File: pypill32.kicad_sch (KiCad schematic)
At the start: 32 parts, among them J1 HeaderR, J2 HeaderL, J3 ISP, U1 SRV05-4, U2 PY32F030F18P6, U3 CH340N

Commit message: intermediate save
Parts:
- removed JP1: PA8_ENA, Jumper:SolderJumper-2_P1.3mm_Open_RoundedPad1.0x1.5mm, symbol Jumper:SolderJumper_2_Open
- added D3: LED-R, LED_SMD:LED_0805_2012Metric_Pad1.15x1.40mm_HandSolder, symbol Device:LED
- added JP2: PA8_SEL, Jumper:SolderJumper-3_P1.3mm_Open_RoundedPad1.0x1.5mm, symbol Jumper:SolderJumper_3_Open
- added R7: 1k, Resistor_SMD:R_0805_2012Metric_Pad1.20x1.40mm_HandSolder, symbol Device:R_Small
- R1: value 1k -> 1.5k
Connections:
- net GND: now also D3.1 (K)
- net PA8: now also JP2.3 (B)
- net at U2.10 (PA8): now also JP2.2 (C)
- net USB_DM renamed USB_D-
- net USB_DP renamed USB_D+
- new net: D3.2 (A), R7.2
- new net: JP2.1 (A), R7.1
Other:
- note added: "TODO: ------ -3V3 regu/hakkuri -BOOT0/1 -nRT-kytkentä -RESET-nappi -ohjelmointiheaderi"

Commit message: intermediate save
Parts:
- removed H1: MountingHole_Pad_MP, MountingHole:MountingHole_2.7mm_M2.5_ISO7380_Pad, symbol Mechanical:MountingHole_Pad_MP
- removed J3: ISP, Connector_PinHeader_2.54mm:PinHeader_1x05_P2.54mm_Vertical, symbol Connector:Conn_01x05_Pin
- added H1: MountingHole, MountingHole:MountingHole_2.7mm_M2.5_ISO7380_Pad, symbol Mechanical:MountingHole
- added J4: ISP, Connector_PinHeader_2.54mm:PinHeader_1x04_P2.54mm_Vertical, symbol Connector:Conn_01x04_Pin
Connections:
- net +3V3: now also J4.4 (Pin_4)
- net GND: now also J4.1 (Pin_1)
- net PF0: now reaches J2.5 (Pin_5), R6.2, U2.1 (OSCIN-PF0)
- net PF1: now reaches J2.6 (Pin_6), R5.2, U2.2 (OSCOUT-PF1)
- net PF2-NRST: now reaches J2.7 (Pin_7), U2.3 (PF2-NRST)
- net PF3: now reaches J2.8 (Pin_8), U2.4 (PF3)
- net PA2: now reaches J2.9 (Pin_9), U2.5 (PA2)
- net PA3: now reaches J2.10 (Pin_10), U2.6 (PA3)
- net PA13 renamed SWDIO
- net SWDIO: now also J4.2 (Pin_2)
- net PA14 renamed SWDCLK
- net SWDCLK: now also J4.3 (Pin_3)
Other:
- note added: "TODO: ------ -SMD fuse -ferriitti? -3V3 regu/hakkuri -BOOT0/1 -nRT-kytkentä -RESET-nappi -alareunan maa ympäri -tarkasta ohjelmointiheaderi -optio 32k kiteelle? -bottomin labelit -ikonit -lisenssi"
- note removed: "TODO: ------ -3V3 regu/hakkuri -BOOT0/1 -nRT-kytkentä -RESET-nappi -ohjelmointiheaderi"

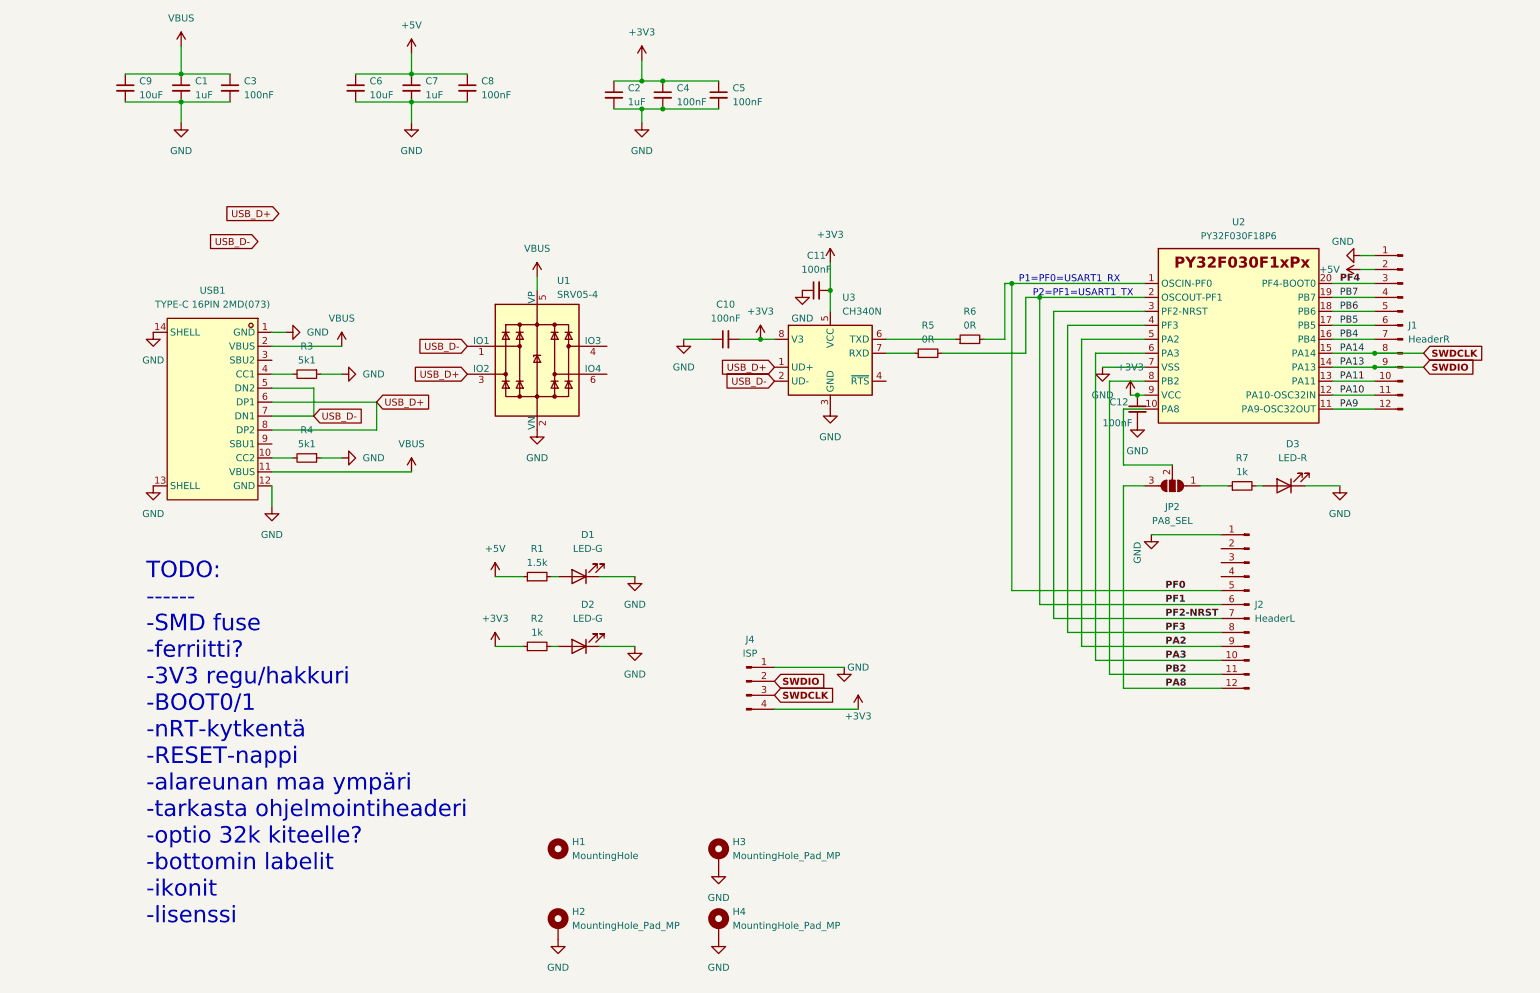
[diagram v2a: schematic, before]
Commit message: switch footprint and 3d
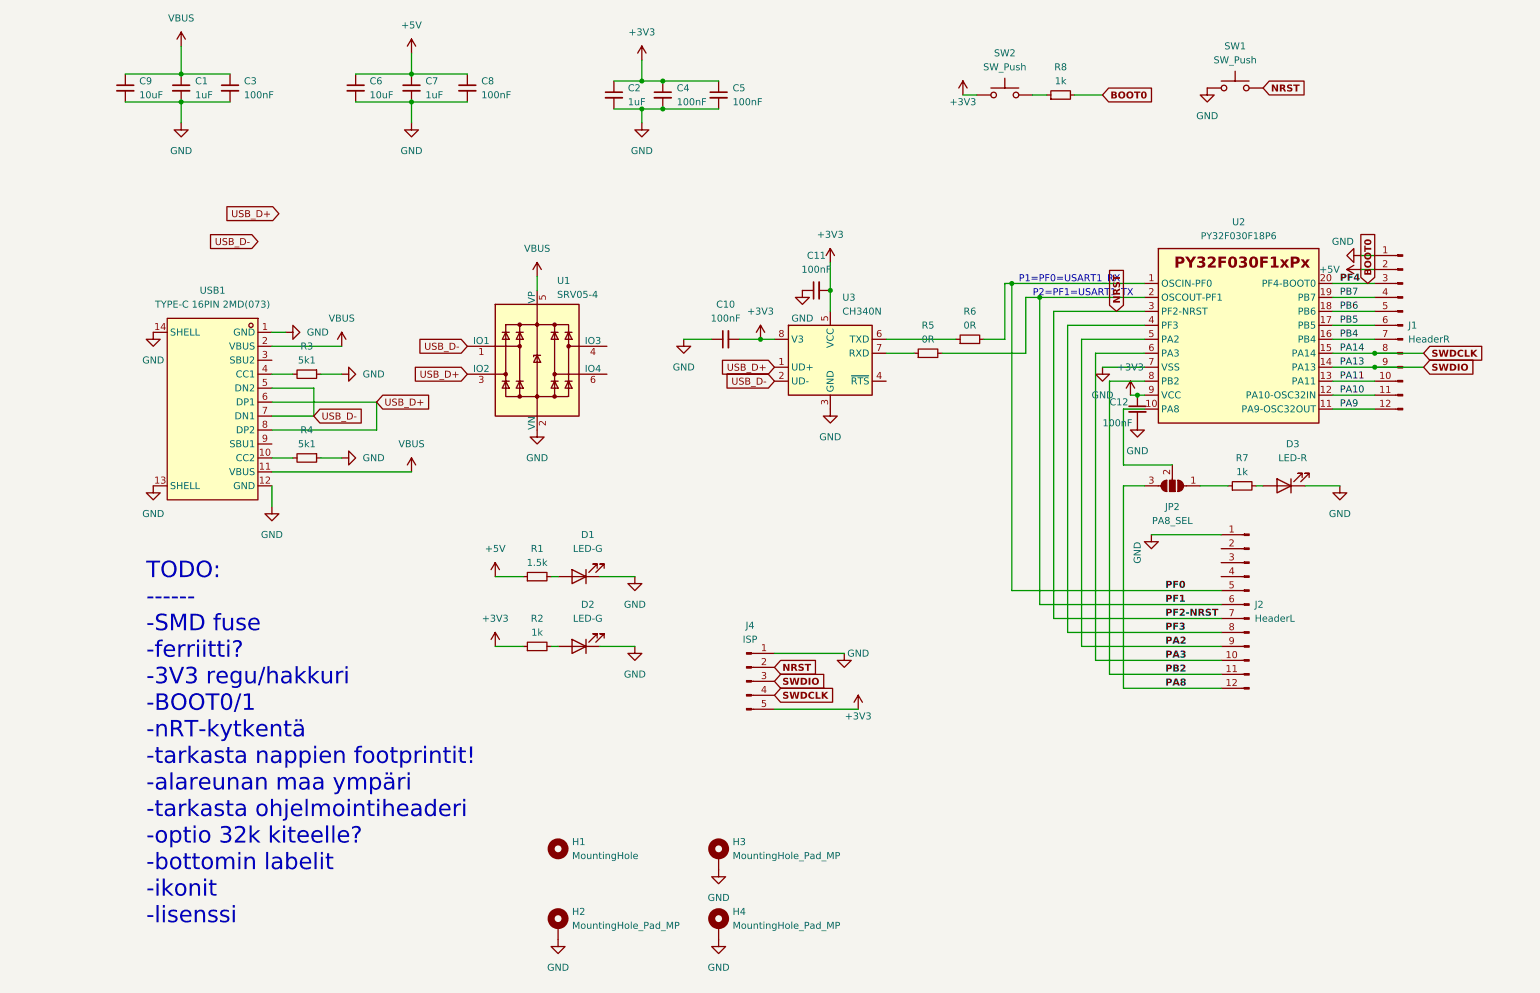
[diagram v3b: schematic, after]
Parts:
- added R8: 1k, Resistor_SMD:R_0805_2012Metric_Pad1.20x1.40mm_HandSolder, symbol Device:R_Small
- added SW1, SW2: SW_Push, pypill32:SW-SMD_L6.0-W3.5-LS8.2, symbol Switch:SW_Push
- J4: footprint Connector_PinHeader_2.54mm:PinHeader_1x04_P2.54mm_Vertical -> Connector_PinHeader_2.54mm:PinHeader_1x05_P2.54mm_Vertical; symbol Connector:Conn_01x04_Pin -> Connector:Conn_01x05_Pin
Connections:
- net +3V3: now also J4.5 (Pin_5), SW2.1; no longer J4.4 (Pin_4)
- net GND: now also SW1.1
- net SWDCLK: now also J4.4 (Pin_4); no longer J4.3 (Pin_3)
- net SWDIO: now also J4.3 (Pin_3); no longer J4.2 (Pin_2)
- net PF2-NRST renamed NRST
- net NRST: now also J4.2 (Pin_2), SW1.2
- net PF4 renamed BOOT0
- net BOOT0: now also R8.2
- new net: R8.1, SW2.2
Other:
- note added: "TODO: ------ -SMD fuse -ferriitti? -3V3 regu/hakkuri -BOOT0/1 -nRT-kytkentä -tarkasta nappien footprintit! -alareunan maa ympäri -tarkasta ohjelmointiheaderi -optio 32k kiteelle? -bottomin labelit -ikonit -lisenssi"
- note removed: "TODO: ------ -SMD fuse -ferriitti? -3V3 regu/hakkuri -BOOT0/1 -nRT-kytkentä -RESET-nappi -alareunan maa ympäri -tarkasta ohjelmointiheaderi -optio 32k kiteelle? -bottomin labelit -ikonit -lisenssi"

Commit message: some progress
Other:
- note added: "TODO: ------ -pinnien selitetekstit isommalle fontille -ruuvireiät maihin -SMD fuse -ferriitti? -USB-pinnireiät? -RGB led? -3V3 regu/hakkuri -tsekkaa BOOT0/1 -nRT-kytkentä -tarkasta nappien footprintit! -alareunan maa ympäri -tarkasta ohjelmointiheaderi -optio 32k kiteelle? -bottomin labelit -2,54 jakoon piikkirimat (protolevylle) -- tasajakoon kiinn.ruuvit -ikonit -lisenssi"
- note removed: "TODO: ------ -SMD fuse -ferriitti? -3V3 regu/hakkuri -BOOT0/1 -nRT-kytkentä -tarkasta nappien footprintit! -alareunan maa ympäri -tarkasta ohjelmointiheaderi -optio 32k kiteelle? -bottomin labelit -ikonit -lisenssi"

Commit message: to be continued
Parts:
- removed C8: 100nF, Capacitor_SMD:C_0805_2012Metric_Pad1.18x1.45mm_HandSolder, symbol Device:C_Small
- H1: symbol Mechanical:MountingHole -> Mechanical:MountingHole_Pad; now left out of the parts list
- H2, H3, H4: value MountingHole_Pad_MP -> MountingHole; symbol Mechanical:MountingHole_Pad_MP -> Mechanical:MountingHole_Pad; now left out of the parts list
- SW1: value SW_Push -> RST_BTN
- SW2: value SW_Push -> BOOT_BTN
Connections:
- net GND: now also H1.1, H2.1, H3.1, H4.1; no longer H2.MP, H3.MP, H4.MP
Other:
- note added: "BOOT0: button pulls it high"
- note added: "RST has internal pull-up -> pulling low causes reset."
- note added: "TODO: ------ -pinnien selitetekstit isommalle fontille -SMD fuse -ferriitti? -USB-pinnireiät? -RGB led? -3V3 regu/hakkuri -kide? -bottomin labelit -2,54 jakoon piikkirimat (protolevylle) -- tasajakoon kiinn.ruuvit -ikonit -lisenssi"
- note removed: "TODO: ------ -pinnien selitetekstit isommalle fontille -ruuvireiät maihin -SMD fuse -ferriitti? -USB-pinnireiät? -RGB led? -3V3 regu/hakkuri -tsekkaa BOOT0/1 -nRT-kytkentä -tarkasta nappien footprintit! -alareunan maa ympäri -tarkasta ohjelmointiheaderi -optio 32k kiteelle? -bottomin labelit -2,54 jakoon piikkirimat (protolevylle) -- tasajakoon kiinn.ruuvit -ikonit -lisenssi"
- moved on the sheet: C1, C3, C6, C7, C9, H3, SW1

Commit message: silks and some routing, to be continued
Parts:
- added C13, C8: 12p TSEKKAA, Capacitor_SMD:C_0805_2012Metric_Pad1.18x1.45mm_HandSolder, symbol Device:C_Small
- added Y1: 32.768 kHz, Crystal:Crystal_Round_D2.0mm_Vertical, symbol Device:Crystal
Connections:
- net +3V3: now also J2.3 (Pin_3)
- net GND: now also J2.4 (Pin_4), C13.2, C8.2
- net PA10: now also C8.1, Y1.2
- net PA9: now also C13.1, Y1.1
- net PWRLED: now reaches D2.2 (A), R2.2
- net PWRLED: now also J2.2 (Pin_2)
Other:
- note added: "TODO: ------ -bottomin tekstit -SMD fuse -ferriitti? -USB-pinnireiät? -RGB led? -3V3 regu/hakkuri -2,54 jakoon piikkirimat (protolevylle) -- tasajakoon kiinn.ruuvit -ikonit -lisenssi"
- note removed: "TODO: ------ -pinnien selitetekstit isommalle fontille -SMD fuse -ferriitti? -USB-pinnireiät? -RGB led? -3V3 regu/hakkuri -kide? -bottomin labelit -2,54 jakoon piikkirimat (protolevylle) -- tasajakoon kiinn.ruuvit -ikonit -lisenssi"

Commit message: further
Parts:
- removed D1: LED-G, LED_SMD:LED_0805_2012Metric_Pad1.15x1.40mm_HandSolder, symbol Device:LED
- removed R1: 1.5k, Resistor_SMD:R_0805_2012Metric_Pad1.20x1.40mm_HandSolder, symbol Device:R_Small
- added C14: 10uF, Capacitor_SMD:C_0805_2012Metric_Pad1.18x1.45mm_HandSolder, symbol Device:C_Small
- added C15: 100nF, Capacitor_SMD:C_0805_2012Metric_Pad1.18x1.45mm_HandSolder, symbol Device:C_Small
- added F1: 0.8A, Fuse:Fuse_1206_3216Metric_Pad1.42x1.75mm_HandSolder, symbol Device:Polyfuse_Small
- added FB1: ~, Inductor_SMD:L_1206_3216Metric_Pad1.42x1.75mm_HandSolder, symbol Device:FerriteBead_Small
- added U4: AMS1117-3.3, Package_TO_SOT_SMD:SOT-223-3_TabPin2, symbol Regulator_Linear:AMS1117-3.3
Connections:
- net +3V3: now also U4.2 (VO)
- net +5V: now also C14.1, C15.1, FB1.2, U4.3 (VI)
- net GND: now also C14.2, C15.2, U4.1 (GND)
- net VBUS: now also F1.1
- new net: F1.2, FB1.1
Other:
- note added: "TODO: ------ -bottomin tekstit -USB-pinnireiät? -2,54 jakoon piikkirimat (protolevylle) -- tasajakoon kiinn.ruuvit -ikonit -lisenssi"
- note removed: "TODO: ------ -bottomin tekstit -SMD fuse -ferriitti? -USB-pinnireiät? -RGB led? -3V3 regu/hakkuri -2,54 jakoon piikkirimat (protolevylle) -- tasajakoon kiinn.ruuvit -ikonit -lisenssi"
- moved on the sheet: C1, C3, C6, C7, C9

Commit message: almost ready
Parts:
- added C16: 10uF, Capacitor_SMD:C_0805_2012Metric_Pad1.18x1.45mm_HandSolder, symbol Device:C_Small
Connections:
- net +3V3: now also C16.1
- net GND: now also C16.2
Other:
- note added: "TODO: ------ -USB-pinnireiät? -2,54 jakoon piikkirimat (protolevylle) -- tasajakoon kiinn.ruuvit"
- note removed: "TODO: ------ -bottomin tekstit -USB-pinnireiät? -2,54 jakoon piikkirimat (protolevylle) -- tasajakoon kiinn.ruuvit -ikonit -lisenssi"
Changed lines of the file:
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@@
 	)
 	(junction
+		(at 125.73 36.83)
+		(diameter 0)
+		(color 0 0 0 0)
+	)
+	(junction
 		(at 264.16 83.82)
 		(diameter 0)
@@
 	)
 	(junction
+		(at 121.92 31.75)
+		(diameter 0)
+		(color 0 0 0 0)
+	)
+	(junction
 		(at 130.81 36.83)
 		(diameter 0)
@@
 	(wire
 		(pts
+			(xy 121.92 36.83) (xy 125.73 36.83)
+		)
+		(stroke
+			(width 0)
+			(type default)
+		)
+	)
+	(wire
+		(pts
 			(xy 41.91 77.47) (xy 41.91 105.41)
 		)
@@
 	(wire
 		(pts
+			(xy 121.92 31.75) (xy 125.73 31.75)
+		)
+		(stroke
+			(width 0)
+			(type default)
+		)
+	)
+	(wire
+		(pts
 			(xy 256.54 86.36) (xy 264.16 86.36)
 		)
@@
 	(wire
 		(pts
-			(xy 119.38 31.75) (xy 125.73 31.75)
+			(xy 119.38 31.75) (xy 121.92 31.75)
 		)
 		(stroke
@@
 		)
 	)
-	(text "TODO: \n------\n-bottomin tekstit\n-USB-pinnireiät?\n-2,54 jakoon piikkirimat (protolevylle) -- tasajakoon kiinn.ruuvit\n-ikonit\n-lisenssi"
+	(text "TODO: \n------\n-USB-pinnireiät?\n-2,54 jakoon piikkirimat \n(protolevylle) -- tasajakoon kiinn.ruuvit\n"
 		(exclude_from_sim no)
-		(at 19.812 187.96 0)
+		(at 22.098 156.464 0)
 		(effects
 			(font
@@
 	)
 	(symbol
+		(lib_id "Device:C_Small")
+		(at 121.92 34.29 0)
+		(unit 1)
+		(exclude_from_sim no)
+		(in_bom yes)
+		(on_board yes)
+		(dnp no)
+		(property "Reference" "C16"
+			(at 120.904 27.94 0)
+			(effects
+				(font
+					(size 1.27 1.27)
+				)
+				(justify left)
+			)
+		)
+		(property "Value" "10uF"
+			(at 120.65 29.718 0)
+			(effects
+				(font
+					(size 1.27 1.27)
+				)
+				(justify left)
+			)
+		)
+		(property "Footprint" "Capacitor_SMD:C_0805_2012Metric_Pad1.18x1.45mm_HandSolder"
+			(at 121.92 34.29 0)
+			(effects
+				(font
+					(size 1.27 1.27)
+				)
+				(hide yes)
+			)
+		)
+		(property "Datasheet" "~"
+			(at 121.92 34.29 0)
+			(effects
+				(font
+					(size 1.27 1.27)
+				)
+				(hide yes)
+			)
+		)
+		(property "Description" ""
+			(at 121.92 34.29 0)
+			(effects
+				(font
+					(size 1.27 1.27)
+				)
+				(hide yes)
+			)
+		)
+		(pin "1"
+		)
+		(pin "2"
+		)
+		(instances
+			(project "pypill32"
+				(path "/0471bd21-091d-469f-a793-0e3efa813f7b"
+					(reference "C16")
+					(unit 1)
+				)
+			)
+		)
+	)
+	(symbol
 		(lib_id "power:+3V3")
 		(at 165.1 64.77 0)
@@
 	(symbol
 		(lib_id "Graphic:Logo_Open_Hardware_Small")
-		(at 21.59 128.27 0)
+		(at 191.77 158.75 0)
 		(unit 1)
 		(exclude_from_sim yes)
@@
 		(fields_autoplaced yes)
 		(property "Reference" "#SYM1"
-			(at 21.59 121.285 0)
+			(at 191.77 151.765 0)
 			(effects
 				(font
@@
 		)
 		(property "Value" "Logo_Open_Hardware_Small"
-			(at 21.59 133.985 0)
+			(at 191.77 164.465 0)
 			(effects
 				(font
@@
 		)
 		(property "Footprint" "Symbol:OSHW-Symbol_6.7x6mm_SilkScreen"
-			(at 21.59 128.27 0)
+			(at 191.77 158.75 0)
 			(effects
 				(font
@@
 		)
 		(property "Datasheet" "~"
-			(at 21.59 128.27 0)
+			(at 191.77 158.75 0)
 			(effects
 				(font
@@
 		)
 		(property "Description" "Open Hardware logo, small"
-			(at 21.59 128.27 0)
+			(at 191.77 158.75 0)
 			(effects
 				(font
